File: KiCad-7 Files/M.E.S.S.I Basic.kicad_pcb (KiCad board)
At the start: 2 copper layers, 32 x 48 mm, 17 parts, among them J1 2383942-4, J2 Molex 0955406888, Q1 PJA3407_R1_00001, U1 SN65LBC179ADR

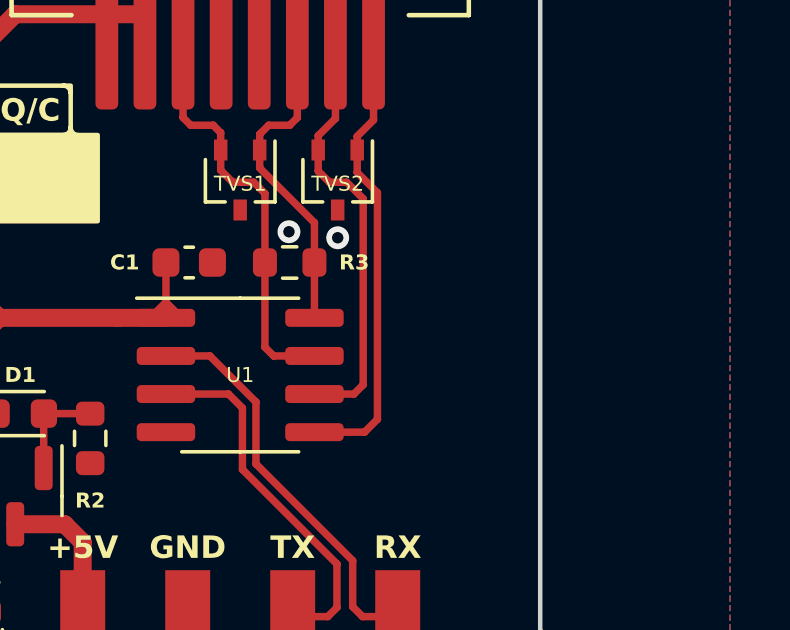
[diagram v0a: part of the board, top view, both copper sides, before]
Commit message: Add files via upload
upload new kicad 7 files with certification mark
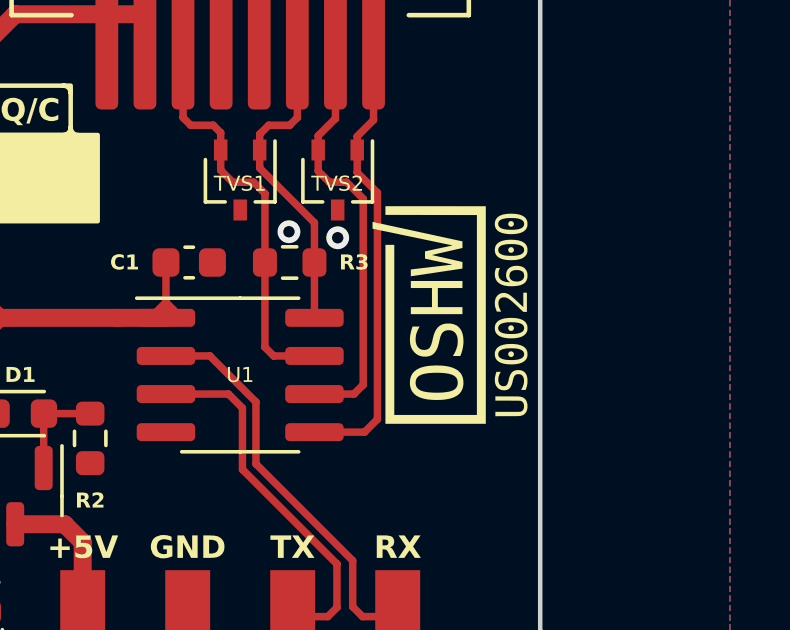
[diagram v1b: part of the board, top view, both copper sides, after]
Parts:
- added G***: LOGO, Custom_Footprints:OSHWA_US002600, F.Cu at (117.0, 78.5)
- D1: value 3V3 -> CZRU52C3V3
- D2: value BLU led -> APTD2012LQBC/D
- J1: value 2383942-4 -> TE 2383942-4
